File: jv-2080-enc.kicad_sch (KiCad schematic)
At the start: 9 parts, among them J1 Conn_01x04, SW1 RotaryEncoder_Switch, U1 ATtiny13A-P

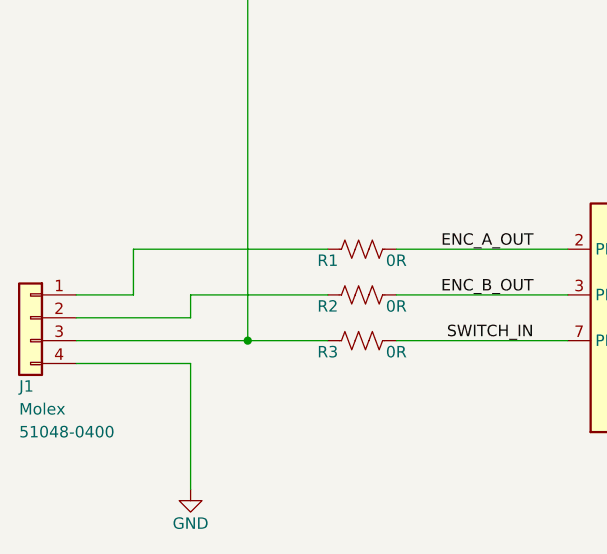
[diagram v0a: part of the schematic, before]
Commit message: Fixed miswired encoder connection. Added helpful silkscreen text. Bumped revision number from 0 to 1.
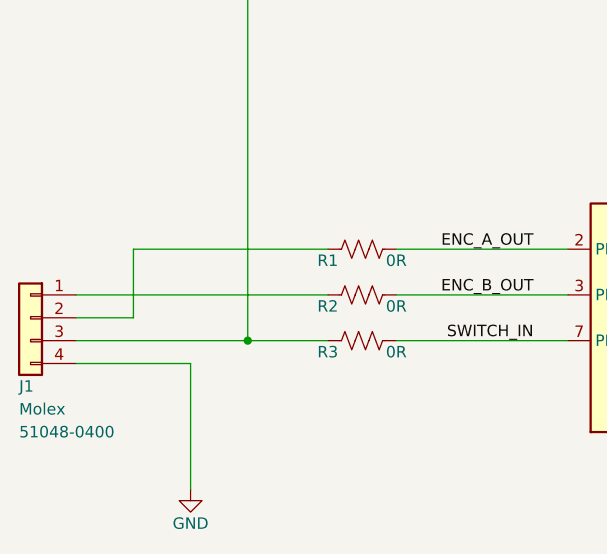
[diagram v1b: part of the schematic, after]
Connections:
- net at J1.1 (Pin_1): now also R2.1; no longer R1.1
- net at J1.2 (Pin_2): now also R1.1; no longer R2.1
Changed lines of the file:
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@@
   (title_block
     (title "REPLACEMENT ENC. BOARD FOR ROLAND 70896167")
-    (date "2022-04-09")
-    (rev "0")
+    (date "2022-05-25")
+    (rev "1")
     (company "Homo Electromagneticus")
   )
@@
   (no_connect (at 154.94 111.76))
   (wire (pts (xy 177.8 99.06) (xy 208.28 99.06))
+    (stroke (width 0) (type default) (color 0 0 0 0))
+  )
+  (wire (pts (xy 69.85 106.68) (xy 76.2 106.68))
     (stroke (width 0) (type default) (color 0 0 0 0))
   )
@@
     (stroke (width 0) (type default) (color 0 0 0 0))
   )
-  (wire (pts (xy 76.2 99.06) (xy 76.2 104.14))
+  (wire (pts (xy 76.2 99.06) (xy 76.2 106.68))
     (stroke (width 0) (type default) (color 0 0 0 0))
   )
@@
     (stroke (width 0) (type default) (color 0 0 0 0))
   )
-  (wire (pts (xy 97.79 104.14) (xy 82.55 104.14))
-    (stroke (width 0) (type default) (color 0 0 0 0))
-  )
-  (wire (pts (xy 69.85 104.14) (xy 76.2 104.14))
+  (wire (pts (xy 69.85 104.14) (xy 97.79 104.14))
     (stroke (width 0) (type default) (color 0 0 0 0))
   )
@@
     (stroke (width 0) (type default) (color 0 0 0 0))
   )
-  (wire (pts (xy 82.55 104.14) (xy 82.55 106.68))
-    (stroke (width 0) (type default) (color 0 0 0 0))
-  )
   (wire (pts (xy 152.4 76.2) (xy 152.4 78.74))
     (stroke (width 0) (type default) (color 0 0 0 0))
@@
     (stroke (width 0) (type default) (color 0 0 0 0))
   )
-  (wire (pts (xy 69.85 106.68) (xy 82.55 106.68))
-    (stroke (width 0) (type default) (color 0 0 0 0))
-  )

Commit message: Added manufacturer and part number details to necessary circuit elements.
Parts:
- C1: Manuf (none) -> Nichicon; Manuf PN (none) -> UVY1E101MDD
- C2, C3: Manuf (none) -> Kemet; Manuf PN (none) -> R82EC1470AA50K
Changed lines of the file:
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@@
       (effects (font (size 1.27 1.27)) hide)
     )
-    (property "Datasheet" "~" (id 3) (at 152.4 82.55 0)
+    (property "Datasheet" "https://www.nichicon.co.jp/english/products/pdfs/e-uvy.pdf" (id 3) (at 152.4 82.55 0)
+      (effects (font (size 1.27 1.27)) hide)
+    )
+    (property "Manuf" "Nichicon" (id 4) (at 152.4 82.55 0)
+      (effects (font (size 1.27 1.27)) hide)
+    )
+    (property "Manuf PN" "UVY1E101MDD" (id 5) (at 152.4 82.55 0)
       (effects (font (size 1.27 1.27)) hide)
     )
@@
       (effects (font (size 1.27 1.27)) hide)
     )
-    (property "Datasheet" "~" (id 3) (at 190.5 114.3 0)
+    (property "Datasheet" "https://content.kemet.com/datasheets/KEM_F3101_R82.pdf" (id 3) (at 190.5 114.3 0)
+      (effects (font (size 1.27 1.27)) hide)
+    )
+    (property "Manuf" "Kemet" (id 4) (at 190.5 114.3 0)
+      (effects (font (size 1.27 1.27)) hide)
+    )
+    (property "Manuf PN" "R82EC1470AA50K" (id 5) (at 190.5 114.3 0)
       (effects (font (size 1.27 1.27)) hide)
     )
@@
       (effects (font (size 1.27 1.27)) hide)
     )
-    (property "Datasheet" "~" (id 3) (at 215.9 94.996 0)
+    (property "Datasheet" "https://www.mouser.ca/datasheet/2/54/PEC11R-777457.pdf" (id 3) (at 215.9 94.996 0)
       (effects (font (size 1.27 1.27)) hide)
     )
@@
       (effects (font (size 1.27 1.27)) hide)
     )
-    (property "Datasheet" "~" (id 3) (at 177.8 114.3 0)
-      (effects (font (size 1.27 1.27)) hide)
-    )
+    (property "Datasheet" "https://content.kemet.com/datasheets/KEM_F3101_R82.pdf" (id 3) (at 177.8 114.3 0)
+      (effects (font (size 1.27 1.27)) hide)
+    )
+    (property "Manuf" "Kemet" (id 4) (at 177.8 114.3 0)
+      (effects (font (size 1.27 1.27)) hide)
+    )
+    (property "Manuf PN" "R82EC1470AA50K" (id 5) (at 177.8 114.3 0)
+      (effects (font (size 1.27 1.27)) hide)
+    )

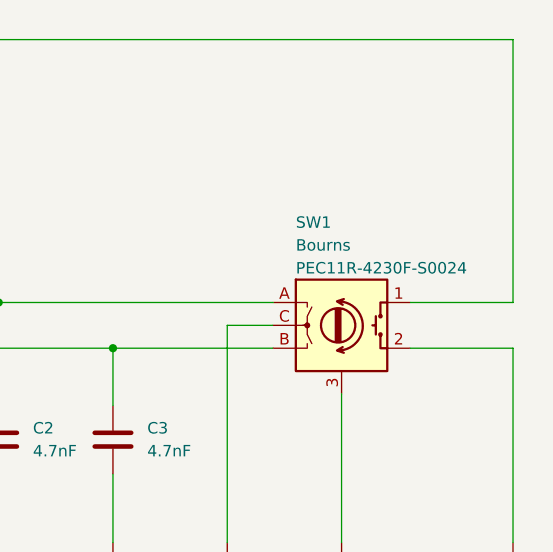
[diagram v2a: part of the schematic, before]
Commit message: Corrected part number of the rotary encoder
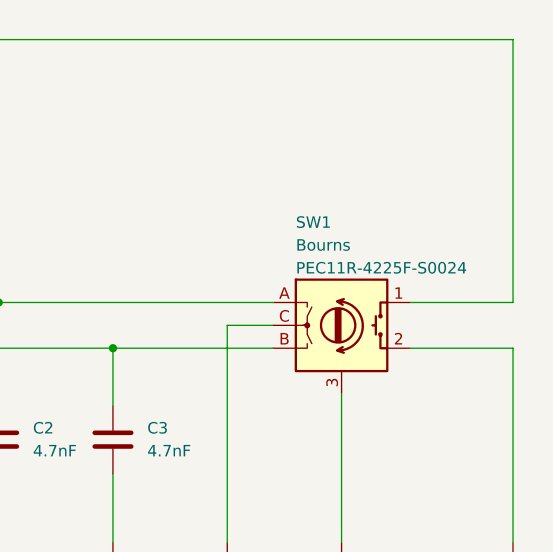
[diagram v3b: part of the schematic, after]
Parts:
- SW1: Manuf PN PEC11R-4230F-S0024 -> PEC11R-4225F-S0024
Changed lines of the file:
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@@
   (title_block
     (title "REPLACEMENT ENC. BOARD FOR ROLAND 70896167")
-    (date "2022-05-25")
+    (date "2022-06-12")
     (rev "1")
     (company "Homo Electromagneticus")
@@
       (effects (font (size 1.27 1.27)) (justify left))
     )
-    (property "Manuf PN" "PEC11R-4230F-S0024" (id 5) (at 210.82 95.25 0)
-      (effects (font (size 1.27 1.27)) (justify left))
-    )
+    (property "Manuf PN" "PEC11R-4225F-S0024" (id 5) (at 210.82 95.25 0)
+      (effects (font (size 1.27 1.27)) (justify left))
+    )
